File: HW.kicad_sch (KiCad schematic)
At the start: 0 parts

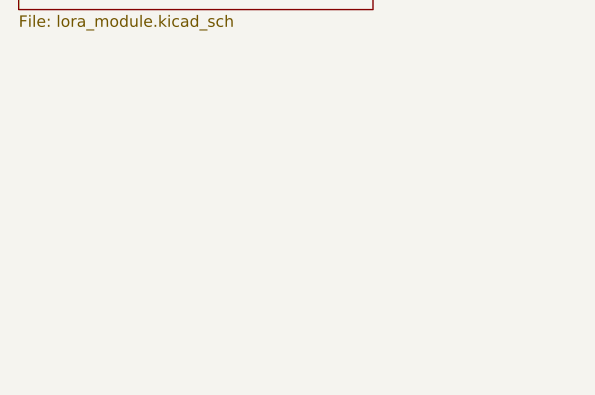
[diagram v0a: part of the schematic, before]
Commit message: feat(power): Add power tree schematic sheet
This commit introduces a new schematic sheet, `power_tree.kicad_sch`, dedicated
to the power distribution network

- This sheet provides a centralized view of the power supply arrangement for
  the entire project.
- It includes voltage regulators, filtering components, and power connections
  to various modules.
- Separating the power tree into its own sheet improves clarity and
  maintainability of the schematic.
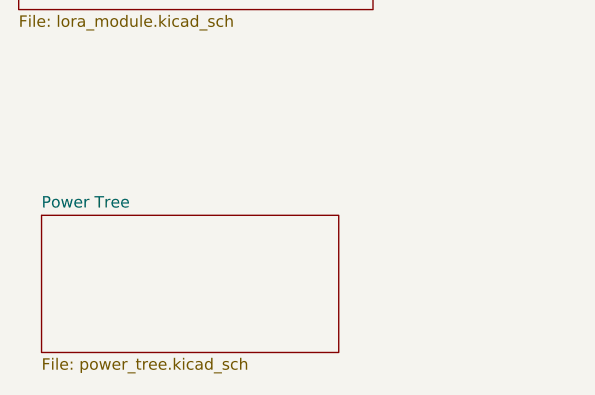
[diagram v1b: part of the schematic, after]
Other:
- added sheet Power Tree (power_tree.kicad_sch)
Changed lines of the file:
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@@
+	)
+	(sheet
+		(at 76.2 148.59)
+		(size 33.02 15.24)
+		(exclude_from_sim no)
+		(in_bom yes)
+		(on_board yes)
+		(dnp no)
+		(fields_autoplaced yes)
+		(stroke
+			(width 0.1524)
+			(type solid)
+		)
+		(fill
+			(color 0 0 0 0.0000)
+		)
+		(property "Sheetname" "Power Tree"
+			(at 76.2 147.8784 0)
+			(effects
+				(font
+					(size 1.27 1.27)
+				)
+				(justify left bottom)
+			)
+		)
+		(property "Sheetfile" "power_tree.kicad_sch"
+			(at 76.2 164.4146 0)
+			(effects
+				(font
+					(size 1.27 1.27)
+				)
+				(justify left top)
+			)
+		)
+		(instances
+			(project "HW"
+				(path "/01550cd7-b424-469c-925b-c370f3609cd4"
+					(page "4")
+				)
+			)
+		)
 	)
 	(sheet

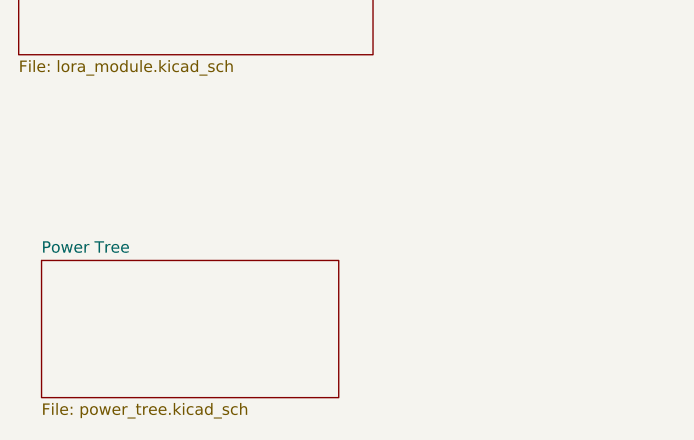
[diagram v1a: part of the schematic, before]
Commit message: feat(power): Add LM1117-based 3.3V voltage regulator
This commit implements a 3.3V voltage regulator circuit using the LM1117
integrated circuit on the `power_tree.kicad_sch` schematic sheet.

- Added the LM1117 component with appropriate input and output capacitors
  as recommended in the datasheet.
- Configured the regulator to provide a stable 3.3V output.
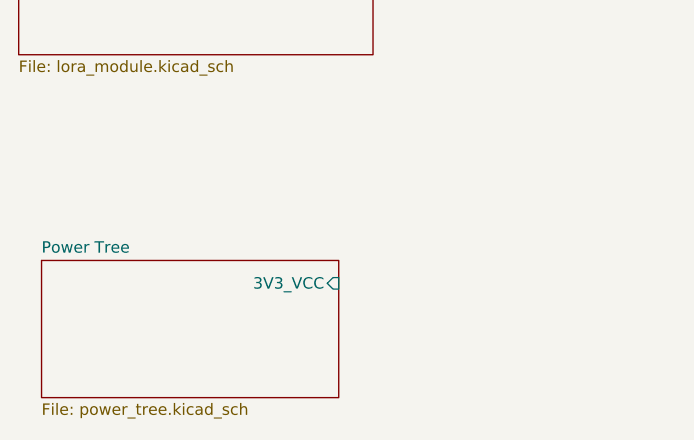
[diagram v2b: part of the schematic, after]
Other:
- sheet Power Tree ports: added 3V3_VCC; removed none
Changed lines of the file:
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@@
+			)
+		)
+		(pin "3V3_VCC" input
+			(at 109.22 151.13 0)
+			(effects
+				(font
+					(size 1.27 1.27)
+				)
+				(justify right)
 			)
 		)

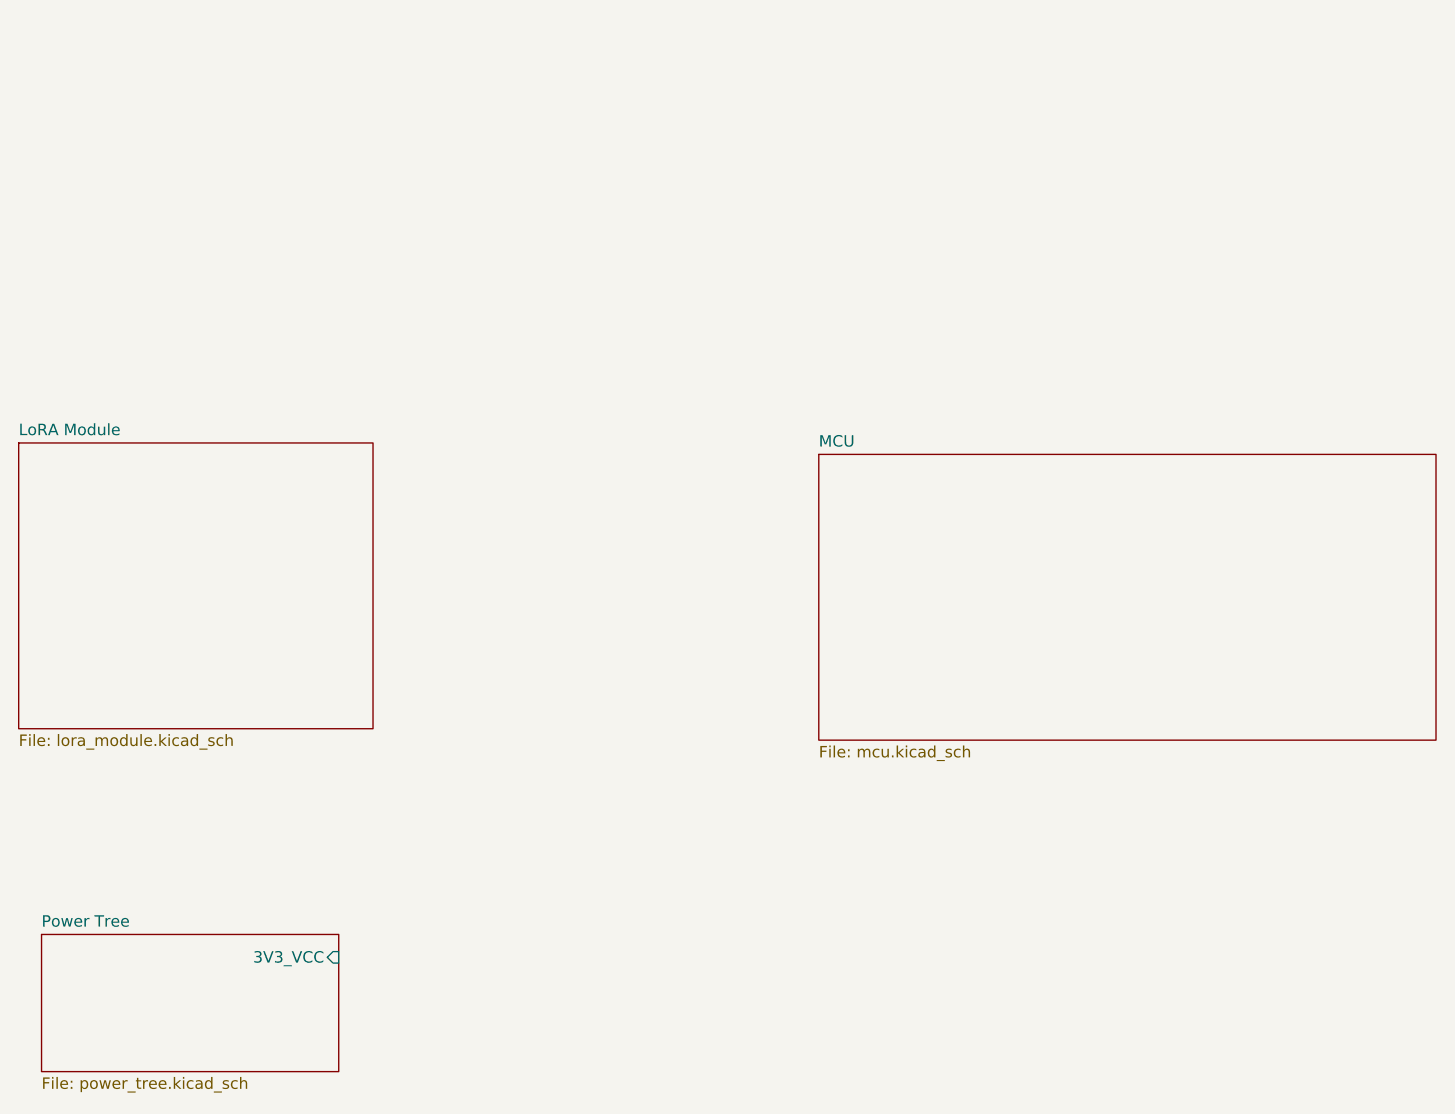
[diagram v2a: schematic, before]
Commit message: fix(power): Connected 3V3_VCC and 3V3_VCCA to VDD and VDDA in MCU
This commit establishes connections between the VCC and VDD pins, as well as
the VCCA and VDDA pins, on the microcontroller unit (MCU).

This resolves a potential issue where the core digital supply (VDD) and the
I/O supply (VCC) were not explicitly linked, and similarly for the analog
supply (VDDA) and analog peripherals supply (VCCA). Connecting these pins
as recommended by the MCU datasheet ensures proper power distribution and
operation of both the digital core and analog peripherals.
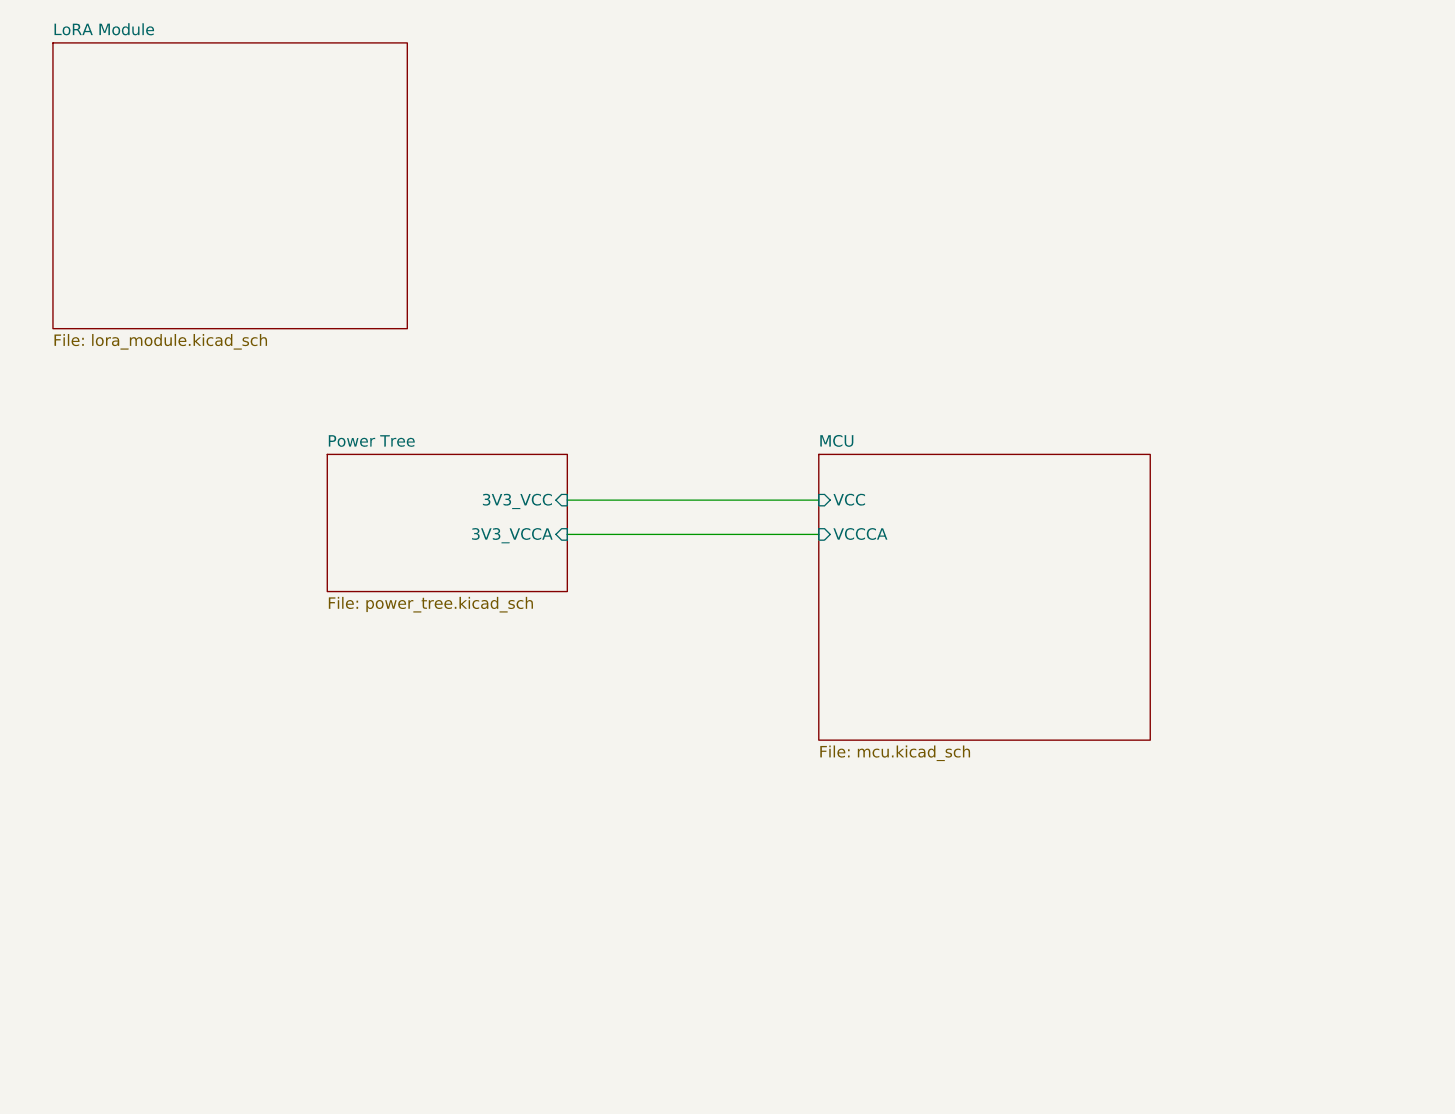
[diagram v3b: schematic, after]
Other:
- sheet MCU ports: added VCC, VCCCA; removed none
- sheet Power Tree ports: added 3V3_VCCA; removed none
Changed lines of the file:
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@@
 	(generator_version "9.0")
 	(paper "A4")
+	(wire
+		(pts
+			(xy 134.62 100.33) (xy 162.56 100.33)
+		)
+		(stroke
+			(width 0)
+			(type default)
+		)
+	)
+	(wire
+		(pts
+			(xy 134.62 104.14) (xy 162.56 104.14)
+		)
+		(stroke
+			(width 0)
+			(type default)
+		)
+	)
 	(sheet
-		(at 73.66 93.98)
+		(at 77.47 49.53)
 		(size 39.37 31.75)
 		(exclude_from_sim no)
@@
 		)
 		(property "Sheetname" "LoRA Module"
-			(at 73.66 93.2684 0)
+			(at 77.47 48.8184 0)
 			(effects
 				(font
@@
 		)
 		(property "Sheetfile" "lora_module.kicad_sch"
-			(at 73.66 126.3146 0)
+			(at 77.47 81.8646 0)
 			(effects
 				(font
@@
 	)
 	(sheet
-		(at 76.2 148.59)
-		(size 33.02 15.24)
+		(at 107.95 95.25)
+		(size 26.67 15.24)
 		(exclude_from_sim no)
 		(in_bom yes)
@@
 		)
 		(property "Sheetname" "Power Tree"
-			(at 76.2 147.8784 0)
+			(at 107.95 94.5384 0)
 			(effects
 				(font
@@
 		)
 		(property "Sheetfile" "power_tree.kicad_sch"
-			(at 76.2 164.4146 0)
+			(at 107.95 111.0746 0)
 			(effects
 				(font
@@
 		)
 		(pin "3V3_VCC" input
-			(at 109.22 151.13 0)
+			(at 134.62 100.33 0)
+			(effects
+				(font
+					(size 1.27 1.27)
+				)
+				(justify right)
+			)
+		)
+		(pin "3V3_VCCA" input
+			(at 134.62 104.14 0)
 			(effects
 				(font
@@
 	(sheet
 		(at 162.56 95.25)
-		(size 68.58 31.75)
+		(size 36.83 31.75)
 		(exclude_from_sim no)
 		(in_bom yes)
@@
 			)
 		)
+		(pin "VCC" input
+			(at 162.56 100.33 180)
+			(effects
+				(font
+					(size 1.27 1.27)
+				)
+				(justify left)
+			)
+		)
+		(pin "VCCCA" input
+			(at 162.56 104.14 180)
+			(effects
+				(font
+					(size 1.27 1.27)
+				)
+				(justify left)
+			)
+		)
